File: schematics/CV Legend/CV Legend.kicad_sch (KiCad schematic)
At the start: 1 part

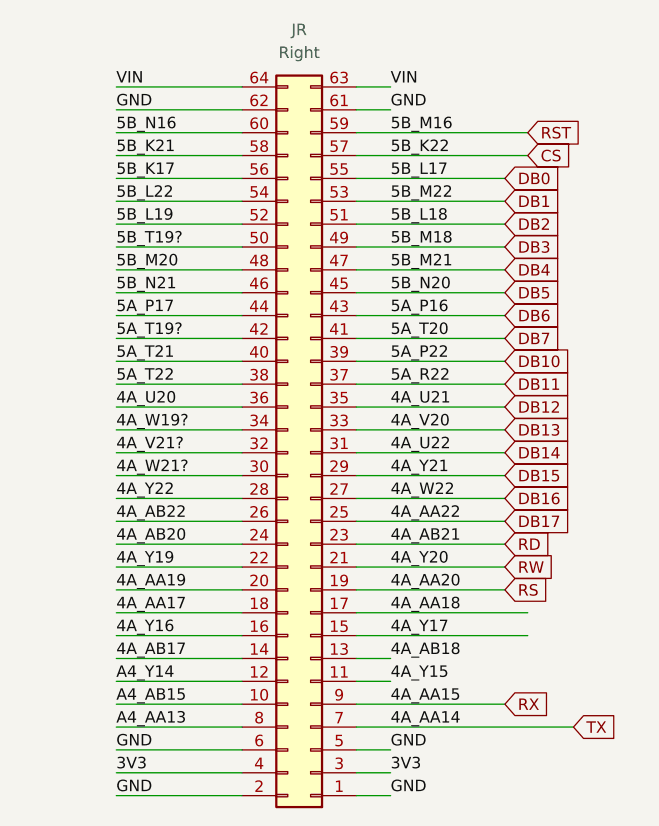
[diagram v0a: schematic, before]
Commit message: Rv32: SPI LCD display working.
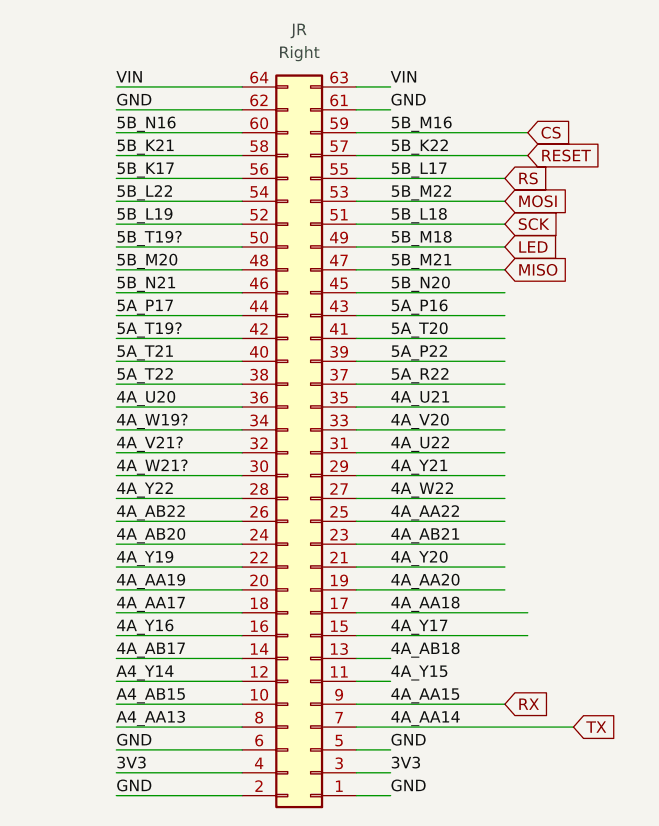
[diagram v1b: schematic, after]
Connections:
- net DB0 is gone; now on net RS: JR.55 (Pin_55)
- net RST is gone; now on net CS: JR.59 (Pin_59)
- net CS: no longer JR.57 (Pin_57)
- net RS: no longer JR.19 (Pin_19)
- net DB1 renamed MOSI
- net DB10 renamed 5A_P22
- net DB11 renamed 5A_R22
- net DB12 renamed 4A_U21
- net DB13 renamed 4A_V20
- net DB14 renamed 4A_U22
- net DB15 renamed 4A_Y21
- net DB16 renamed 4A_W22
- net DB17 renamed 4A_AA22
- net DB2 renamed SCK
- net DB3 renamed LED
- net DB4 renamed MISO
- net DB5 renamed 5B_N20
- net DB6 renamed 5A_P16
- net DB7 renamed 5A_T20
- net RD renamed 4A_AB21
- net RW renamed 4A_Y20
- new net 4A_AA20: JR.19 (Pin_19)
- new net RESET: JR.57 (Pin_57)
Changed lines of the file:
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@@
     (effects (font (size 1.27 1.27)) (justify left bottom))
   )
-  (global_label "DB10" (shape input) (at 140.97 74.93 0) (fields_autoplaced)
+  (global_label "MISO" (shape input) (at 140.97 64.77 0) (fields_autoplaced)
     (effects (font (size 1.27 1.27)) (justify left))
-    (property "Intersheet References" "${INTERSHEET_REFS}" (id 0) (at 148.3421 74.8506 0)
+    (property "Intersheet References" "${INTERSHEET_REFS}" (id 0) (at 147.9793 64.6906 0)
       (effects (font (size 1.27 1.27)) (justify left) hide)
     )
   )
-  (global_label "DB4" (shape input) (at 140.97 64.77 0) (fields_autoplaced)
+  (global_label "CS" (shape input) (at 143.51 49.53 0) (fields_autoplaced)
     (effects (font (size 1.27 1.27)) (justify left))
-    (property "Intersheet References" "${INTERSHEET_REFS}" (id 0) (at 147.1326 64.6906 0)
-      (effects (font (size 1.27 1.27)) (justify left) hide)
-    )
-  )
-  (global_label "RST" (shape input) (at 143.51 49.53 0) (fields_autoplaced)
-    (effects (font (size 1.27 1.27)) (justify left))
-    (property "Intersheet References" "${INTERSHEET_REFS}" (id 0) (at 149.3702 49.4506 0)
+    (property "Intersheet References" "${INTERSHEET_REFS}" (id 0) (at 148.4026 49.4506 0)
       (effects (font (size 1.27 1.27)) (justify left) hide)
     )
@@
     )
   )
-  (global_label "DB0" (shape input) (at 140.97 54.61 0) (fields_autoplaced)
+  (global_label "RS" (shape input) (at 140.97 54.61 0) (fields_autoplaced)
     (effects (font (size 1.27 1.27)) (justify left))
-    (property "Intersheet References" "${INTERSHEET_REFS}" (id 0) (at 147.1326 54.5306 0)
+    (property "Intersheet References" "${INTERSHEET_REFS}" (id 0) (at 145.8626 54.5306 0)
       (effects (font (size 1.27 1.27)) (justify left) hide)
     )
   )
-  (global_label "DB12" (shape input) (at 140.97 80.01 0) (fields_autoplaced)
-    (effects (font (size 1.27 1.27)) (justify left))
-    (property "Intersheet References" "${INTERSHEET_REFS}" (id 0) (at 148.3421 79.9306 0)
-      (effects (font (size 1.27 1.27)) (justify left) hide)
-    )
-  )
-  (global_label "DB5" (shape input) (at 140.97 67.31 0) (fields_autoplaced)
-    (effects (font (size 1.27 1.27)) (justify left))
-    (property "Intersheet References" "${INTERSHEET_REFS}" (id 0) (at 147.1326 67.2306 0)
-      (effects (font (size 1.27 1.27)) (justify left) hide)
-    )
-  )
-  (global_label "DB15" (shape input) (at 140.97 87.63 0) (fields_autoplaced)
-    (effects (font (size 1.27 1.27)) (justify left))
-    (property "Intersheet References" "${INTERSHEET_REFS}" (id 0) (at 148.3421 87.5506 0)
-      (effects (font (size 1.27 1.27)) (justify left) hide)
-    )
-  )
-  (global_label "DB2" (shape input) (at 140.97 59.69 0) (fields_autoplaced)
+  (global_label "SCK" (shape input) (at 140.97 59.69 0) (fields_autoplaced)
     (effects (font (size 1.27 1.27)) (justify left))
     (property "Intersheet References" "${INTERSHEET_REFS}" (id 0) (at 147.1326 59.6106 0)
@@
     )
   )
-  (global_label "DB7" (shape input) (at 140.97 72.39 0) (fields_autoplaced)
+  (global_label "RESET" (shape input) (at 143.51 52.07 0) (fields_autoplaced)
     (effects (font (size 1.27 1.27)) (justify left))
-    (property "Intersheet References" "${INTERSHEET_REFS}" (id 0) (at 147.1326 72.3106 0)
+    (property "Intersheet References" "${INTERSHEET_REFS}" (id 0) (at 151.6683 51.9906 0)
       (effects (font (size 1.27 1.27)) (justify left) hide)
     )
   )
-  (global_label "DB6" (shape input) (at 140.97 69.85 0) (fields_autoplaced)
+  (global_label "MOSI" (shape input) (at 140.97 57.15 0) (fields_autoplaced)
     (effects (font (size 1.27 1.27)) (justify left))
-    (property "Intersheet References" "${INTERSHEET_REFS}" (id 0) (at 147.1326 69.7706 0)
-      (effects (font (size 1.27 1.27)) (justify left) hide)
-    )
-  )
-  (global_label "DB16" (shape input) (at 140.97 90.17 0) (fields_autoplaced)
-    (effects (font (size 1.27 1.27)) (justify left))
-    (property "Intersheet References" "${INTERSHEET_REFS}" (id 0) (at 148.3421 90.0906 0)
-      (effects (font (size 1.27 1.27)) (justify left) hide)
-    )
-  )
-  (global_label "RW" (shape input) (at 140.97 97.79 0) (fields_autoplaced)
-    (effects (font (size 1.27 1.27)) (justify left))
-    (property "Intersheet References" "${INTERSHEET_REFS}" (id 0) (at 146.1045 97.7106 0)
-      (effects (font (size 1.27 1.27)) (justify left) hide)
-    )
-  )
-  (global_label "DB17" (shape input) (at 140.97 92.71 0) (fields_autoplaced)
-    (effects (font (size 1.27 1.27)) (justify left))
-    (property "Intersheet References" "${INTERSHEET_REFS}" (id 0) (at 148.3421 92.6306 0)
-      (effects (font (size 1.27 1.27)) (justify left) hide)
-    )
-  )
-  (global_label "CS" (shape input) (at 143.51 52.07 0) (fields_autoplaced)
-    (effects (font (size 1.27 1.27)) (justify left))
-    (property "Intersheet References" "${INTERSHEET_REFS}" (id 0) (at 148.4026 51.9906 0)
-      (effects (font (size 1.27 1.27)) (justify left) hide)
-    )
-  )
-  (global_label "DB1" (shape input) (at 140.97 57.15 0) (fields_autoplaced)
-    (effects (font (size 1.27 1.27)) (justify left))
-    (property "Intersheet References" "${INTERSHEET_REFS}" (id 0) (at 147.1326 57.0706 0)
-      (effects (font (size 1.27 1.27)) (justify left) hide)
-    )
-  )
-  (global_label "DB11" (shape input) (at 140.97 77.47 0) (fields_autoplaced)
-    (effects (font (size 1.27 1.27)) (justify left))
-    (property "Intersheet References" "${INTERSHEET_REFS}" (id 0) (at 148.3421 77.3906 0)
-      (effects (font (size 1.27 1.27)) (justify left) hide)
-    )
-  )
-  (global_label "DB13" (shape input) (at 140.97 82.55 0) (fields_autoplaced)
-    (effects (font (size 1.27 1.27)) (justify left))
-    (property "Intersheet References" "${INTERSHEET_REFS}" (id 0) (at 148.3421 82.4706 0)
+    (property "Intersheet References" "${INTERSHEET_REFS}" (id 0) (at 147.9793 57.0706 0)
       (effects (font (size 1.27 1.27)) (justify left) hide)
     )
@@
     )
   )
-  (global_label "DB14" (shape input) (at 140.97 85.09 0) (fields_autoplaced)
+  (global_label "LED" (shape input) (at 140.97 62.23 0) (fields_autoplaced)
     (effects (font (size 1.27 1.27)) (justify left))
-    (property "Intersheet References" "${INTERSHEET_REFS}" (id 0) (at 148.3421 85.0106 0)
+    (property "Intersheet References" "${INTERSHEET_REFS}" (id 0) (at 146.8302 62.1506 0)
       (effects (font (size 1.27 1.27)) (justify left) hide)
     )
-  )
-  (global_label "RS" (shape input) (at 140.97 100.33 0) (fields_autoplaced)
-    (effects (font (size 1.27 1.27)) (justify left))
-    (property "Intersheet References" "${INTERSHEET_REFS}" (id 0) (at 145.8626 100.2506 0)
-      (effects (font (size 1.27 1.27)) (justify left) hide)
-    )
-  )
-  (global_label "RD" (shape input) (at 140.97 95.25 0) (fields_autoplaced)
-    (effects (font (size 1.27 1.27)) (justify left))
-    (property "Intersheet References" "${INTERSHEET_REFS}" (id 0) (at 145.9231 95.1706 0)
-      (effects (font (size 1.27 1.27)) (justify left) hide)
-    )
-  )
-  (global_label "DB3" (shape input) (at 140.97 62.23 0) (fields_autoplaced)
-    (effects (font (size 1.27 1.27)) (justify left))
-    (property "Intersheet References" "${INTERSHEET_REFS}" (id 0) (at 147.1326 62.1506 0)
-      (effects (font (size 1.27 1.27)) (justify left) hide)
-    )

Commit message: Rv32: Some schematics work.
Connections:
- net 4A_AA20 renamed LCD_G7
- net 4A_AA22 renamed LCD_G4
- net 4A_AB21 renamed LCD_G5
- net 4A_U21 renamed LCD_R7
- net 4A_U22 renamed LCD_G1
- net 4A_V20 renamed LCD_G0
- net 4A_W22 renamed LCD_G3
- net 4A_Y20 renamed LCD_G6
- net 4A_Y21 renamed LCD_G2
- net 5A_P16 renamed LCD_R3
- net 5A_P22 renamed LCD_R5
- net 5A_R22 renamed LCD_R6
- net 5A_T20 renamed LCD_R4
- net 5B_K17 renamed LCD_B2
- net 5B_K21 renamed LCD_B1
- net 5B_L19 renamed LCD_B4
- net 5B_L22 renamed LCD_B3
- net 5B_M20 renamed LCD_B6
- net 5B_N16 renamed LCD_B0
- net 5B_N20 renamed LCD_R2
- net 5B_N21 renamed LCD_B7
- net 5B_T19? renamed LCD_B5
- net CS renamed LCD_BKL
- net LED renamed LCD_R0
- net MISO renamed LCD_R1
- net MOSI renamed LCD_VSYNC
- net RESET renamed LCD_CLK
- net RS renamed LCD_HSYNC
- net SCK renamed LCD_DE
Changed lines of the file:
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@@
     (effects (font (size 1.27 1.27)) (justify left bottom))
   )
-  (global_label "MISO" (shape input) (at 140.97 64.77 0) (fields_autoplaced)
+  (global_label "LCD_B3" (shape input) (at 97.79 57.15 180) (fields_autoplaced)
+    (effects (font (size 1.27 1.27)) (justify right))
+    (property "Intersheet References" "${INTERSHEET_REFS}" (id 0) (at 88.3617 57.0706 0)
+      (effects (font (size 1.27 1.27)) (justify right) hide)
+    )
+  )
+  (global_label "LCD_R3" (shape input) (at 140.97 69.85 0) (fields_autoplaced)
     (effects (font (size 1.27 1.27)) (justify left))
-    (property "Intersheet References" "${INTERSHEET_REFS}" (id 0) (at 147.9793 64.6906 0)
+    (property "Intersheet References" "${INTERSHEET_REFS}" (id 0) (at 150.3983 69.7706 0)
       (effects (font (size 1.27 1.27)) (justify left) hide)
     )
   )
-  (global_label "CS" (shape input) (at 143.51 49.53 0) (fields_autoplaced)
+  (global_label "LCD_G4" (shape input) (at 140.97 92.71 0) (fields_autoplaced)
     (effects (font (size 1.27 1.27)) (justify left))
-    (property "Intersheet References" "${INTERSHEET_REFS}" (id 0) (at 148.4026 49.4506 0)
+    (property "Intersheet References" "${INTERSHEET_REFS}" (id 0) (at 150.3983 92.6306 0)
+      (effects (font (size 1.27 1.27)) (justify left) hide)
+    )
+  )
+  (global_label "LCD_R6" (shape input) (at 140.97 77.47 0) (fields_autoplaced)
+    (effects (font (size 1.27 1.27)) (justify left))
+    (property "Intersheet References" "${INTERSHEET_REFS}" (id 0) (at 150.3983 77.3906 0)
+      (effects (font (size 1.27 1.27)) (justify left) hide)
+    )
+  )
+  (global_label "LCD_G0" (shape input) (at 140.97 82.55 0) (fields_autoplaced)
+    (effects (font (size 1.27 1.27)) (justify left))
+    (property "Intersheet References" "${INTERSHEET_REFS}" (id 0) (at 150.3983 82.4706 0)
+      (effects (font (size 1.27 1.27)) (justify left) hide)
+    )
+  )
+  (global_label "LCD_BKL" (shape input) (at 143.51 49.53 0) (fields_autoplaced)
+    (effects (font (size 1.27 1.27)) (justify left))
+    (property "Intersheet References" "${INTERSHEET_REFS}" (id 0) (at 154.0269 49.4506 0)
       (effects (font (size 1.27 1.27)) (justify left) hide)
     )
@@
     )
   )
-  (global_label "RS" (shape input) (at 140.97 54.61 0) (fields_autoplaced)
+  (global_label "LCD_R0" (shape input) (at 140.97 62.23 0) (fields_autoplaced)
     (effects (font (size 1.27 1.27)) (justify left))
-    (property "Intersheet References" "${INTERSHEET_REFS}" (id 0) (at 145.8626 54.5306 0)
+    (property "Intersheet References" "${INTERSHEET_REFS}" (id 0) (at 150.3983 62.1506 0)
       (effects (font (size 1.27 1.27)) (justify left) hide)
     )
   )
-  (global_label "SCK" (shape input) (at 140.97 59.69 0) (fields_autoplaced)
+  (global_label "LCD_HSYNC" (shape input) (at 140.97 54.61 0) (fields_autoplaced)
     (effects (font (size 1.27 1.27)) (justify left))
-    (property "Intersheet References" "${INTERSHEET_REFS}" (id 0) (at 147.1326 59.6106 0)
+    (property "Intersheet References" "${INTERSHEET_REFS}" (id 0) (at 154.1479 54.5306 0)
       (effects (font (size 1.27 1.27)) (justify left) hide)
     )
   )
-  (global_label "RESET" (shape input) (at 143.51 52.07 0) (fields_autoplaced)
+  (global_label "LCD_G3" (shape input) (at 140.97 90.17 0) (fields_autoplaced)
     (effects (font (size 1.27 1.27)) (justify left))
-    (property "Intersheet References" "${INTERSHEET_REFS}" (id 0) (at 151.6683 51.9906 0)
+    (property "Intersheet References" "${INTERSHEET_REFS}" (id 0) (at 150.3983 90.0906 0)
       (effects (font (size 1.27 1.27)) (justify left) hide)
     )
   )
-  (global_label "MOSI" (shape input) (at 140.97 57.15 0) (fields_autoplaced)
+  (global_label "LCD_B1" (shape input) (at 97.79 52.07 180) (fields_autoplaced)
+    (effects (font (size 1.27 1.27)) (justify right))
+    (property "Intersheet References" "${INTERSHEET_REFS}" (id 0) (at 88.3617 51.9906 0)
+      (effects (font (size 1.27 1.27)) (justify right) hide)
+    )
+  )
+  (global_label "LCD_R7" (shape input) (at 140.97 80.01 0) (fields_autoplaced)
     (effects (font (size 1.27 1.27)) (justify left))
-    (property "Intersheet References" "${INTERSHEET_REFS}" (id 0) (at 147.9793 57.0706 0)
+    (property "Intersheet References" "${INTERSHEET_REFS}" (id 0) (at 150.3983 79.9306 0)
       (effects (font (size 1.27 1.27)) (justify left) hide)
+    )
+  )
+  (global_label "LCD_DE" (shape input) (at 140.97 59.69 0) (fields_autoplaced)
+    (effects (font (size 1.27 1.27)) (justify left))
+    (property "Intersheet References" "${INTERSHEET_REFS}" (id 0) (at 150.3379 59.6106 0)
+      (effects (font (size 1.27 1.27)) (justify left) hide)
+    )
+  )
+  (global_label "LCD_G2" (shape input) (at 140.97 87.63 0) (fields_autoplaced)
+    (effects (font (size 1.27 1.27)) (justify left))
+    (property "Intersheet References" "${INTERSHEET_REFS}" (id 0) (at 150.3983 87.5506 0)
+      (effects (font (size 1.27 1.27)) (justify left) hide)
+    )
+  )
+  (global_label "LCD_R5" (shape input) (at 140.97 74.93 0) (fields_autoplaced)
+    (effects (font (size 1.27 1.27)) (justify left))
+    (property "Intersheet References" "${INTERSHEET_REFS}" (id 0) (at 150.3983 74.8506 0)
+      (effects (font (size 1.27 1.27)) (justify left) hide)
+    )
+  )
+  (global_label "LCD_B5" (shape input) (at 97.79 62.23 180) (fields_autoplaced)
+    (effects (font (size 1.27 1.27)) (justify right))
+    (property "Intersheet References" "${INTERSHEET_REFS}" (id 0) (at 88.3617 62.1506 0)
+      (effects (font (size 1.27 1.27)) (justify right) hide)
+    )
+  )
+  (global_label "LCD_CLK" (shape input) (at 143.51 52.07 0) (fields_autoplaced)
+    (effects (font (size 1.27 1.27)) (justify left))
+    (property "Intersheet References" "${INTERSHEET_REFS}" (id 0) (at 154.0269 51.9906 0)
+      (effects (font (size 1.27 1.27)) (justify left) hide)
+    )
+  )
+  (global_label "LCD_G6" (shape input) (at 140.97 97.79 0) (fields_autoplaced)
+    (effects (font (size 1.27 1.27)) (justify left))
+    (property "Intersheet References" "${INTERSHEET_REFS}" (id 0) (at 150.3983 97.7106 0)
+      (effects (font (size 1.27 1.27)) (justify left) hide)
+    )
+  )
+  (global_label "LCD_VSYNC" (shape input) (at 140.97 57.15 0) (fields_autoplaced)
+    (effects (font (size 1.27 1.27)) (justify left))
+    (property "Intersheet References" "${INTERSHEET_REFS}" (id 0) (at 153.906 57.0706 0)
+      (effects (font (size 1.27 1.27)) (justify left) hide)
+    )
+  )
+  (global_label "LCD_B0" (shape input) (at 97.79 49.53 180) (fields_autoplaced)
+    (effects (font (size 1.27 1.27)) (justify right))
+    (property "Intersheet References" "${INTERSHEET_REFS}" (id 0) (at 88.3617 49.4506 0)
+      (effects (font (size 1.27 1.27)) (justify right) hide)
+    )
+  )
+  (global_label "LCD_B7" (shape input) (at 97.79 67.31 180) (fields_autoplaced)
+    (effects (font (size 1.27 1.27)) (justify right))
+    (property "Intersheet References" "${INTERSHEET_REFS}" (id 0) (at 88.3617 67.2306 0)
+      (effects (font (size 1.27 1.27)) (justify right) hide)
+    )
+  )
+  (global_label "LCD_R2" (shape input) (at 140.97 67.31 0) (fields_autoplaced)
+    (effects (font (size 1.27 1.27)) (justify left))
+    (property "Intersheet References" "${INTERSHEET_REFS}" (id 0) (at 150.3983 67.2306 0)
+      (effects (font (size 1.27 1.27)) (justify left) hide)
+    )
+  )
+  (global_label "LCD_B4" (shape input) (at 97.79 59.69 180) (fields_autoplaced)
+    (effects (font (size 1.27 1.27)) (justify right))
+    (property "Intersheet References" "${INTERSHEET_REFS}" (id 0) (at 88.3617 59.6106 0)
+      (effects (font (size 1.27 1.27)) (justify right) hide)
     )
   )
@@
     )
   )
-  (global_label "LED" (shape input) (at 140.97 62.23 0) (fields_autoplaced)
+  (global_label "LCD_G5" (shape input) (at 140.97 95.25 0) (fields_autoplaced)
     (effects (font (size 1.27 1.27)) (justify left))
-    (property "Intersheet References" "${INTERSHEET_REFS}" (id 0) (at 146.8302 62.1506 0)
+    (property "Intersheet References" "${INTERSHEET_REFS}" (id 0) (at 150.3983 95.1706 0)
       (effects (font (size 1.27 1.27)) (justify left) hide)
     )
+  )
+  (global_label "LCD_G1" (shape input) (at 140.97 85.09 0) (fields_autoplaced)
+    (effects (font (size 1.27 1.27)) (justify left))
+    (property "Intersheet References" "${INTERSHEET_REFS}" (id 0) (at 150.3983 85.0106 0)
+      (effects (font (size 1.27 1.27)) (justify left) hide)
+    )
+  )
+  (global_label "LCD_B2" (shape input) (at 97.79 54.61 180) (fields_autoplaced)
+    (effects (font (size 1.27 1.27)) (justify right))
+    (property "Intersheet References" "${INTERSHEET_REFS}" (id 0) (at 88.3617 54.5306 0)
+      (effects (font (size 1.27 1.27)) (justify right) hide)
+    )
+  )
+  (global_label "LCD_B6" (shape input) (at 97.79 64.77 180) (fields_autoplaced)
+    (effects (font (size 1.27 1.27)) (justify right))
+    (property "Intersheet References" "${INTERSHEET_REFS}" (id 0) (at 88.3617 64.6906 0)
+      (effects (font (size 1.27 1.27)) (justify right) hide)
+    )
+  )
+  (global_label "LCD_G7" (shape input) (at 140.97 100.33 0) (fields_autoplaced)
+    (effects (font (size 1.27 1.27)) (justify left))
+    (property "Intersheet References" "${INTERSHEET_REFS}" (id 0) (at 150.3983 100.2506 0)
+      (effects (font (size 1.27 1.27)) (justify left) hide)
+    )
+  )
+  (global_label "LCD_R4" (shape input) (at 140.97 72.39 0) (fields_autoplaced)
+    (effects (font (size 1.27 1.27)) (justify left))
+    (property "Intersheet References" "${INTERSHEET_REFS}" (id 0) (at 150.3983 72.3106 0)
+      (effects (font (size 1.27 1.27)) (justify left) hide)
+    )
+  )
+  (global_label "LCD_R1" (shape input) (at 140.97 64.77 0) (fields_autoplaced)
+    (effects (font (size 1.27 1.27)) (justify left))
+    (property "Intersheet References" "${INTERSHEET_REFS}" (id 0) (at 150.3983 64.6906 0)
+      (effects (font (size 1.27 1.27)) (justify left) hide)
+    )
